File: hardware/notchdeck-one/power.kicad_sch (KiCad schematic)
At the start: 23 parts, among them J1 USB-C, J2 BAT 1S, Q1 AO3401A, U2 AP2112K-3.3, U3 MCP73832-2-OT, U4 MAX17048, U7 USBLC6-2SC6

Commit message: Add keyed harnesses and build plan for Japanese-style dual and mascon handles
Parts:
- J2: BOM Comments Mating harnesses not included. J2: protected 1S cell, pin 1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 -> Two-pin JST PH battery connector. Pin1=BAT+, pin2=GND. Mati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
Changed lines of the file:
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@@
 		(title "NotchDeck One — Power and battery")
 		(date "2026-10-03")
-		(rev "C")
+		(rev "D")
 		(company "BenchBits")
 	)
@@
 			(effects (font (size 1.27 1.27))) (hide yes)
 		)
-		(property "BOM Comments" "Mating harnesses not included. J2: protected 1S cell, pin 1 positive / pin 2 ground. J5-J8: lever signal / ground."
+		(property "BOM Comments" "Two-pin JST PH battery connector. Pin1=BAT+, pin2=GND. Mating harness separate."
 			(at 182.8800 167.6400 0)
 			(effects (font (size 1.27 1.27))) (hide yes)

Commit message: Add protected PWM actuator outputs and charger interlock
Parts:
- added Q6: 2N7002, Package_TO_SOT_SMD:SOT-23, symbol Transistor_FET:2N7002
- added R59: 100k, Resistor_SMD:R_0402_1005Metric, symbol Device:R
- J2: BOM Checked 2026-10-03 -> 2026-10-05
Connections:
- net +3V3: now also R59.1
- net GND: now also Q6.2 (S); no longer R3.2
- net BAT+ renamed BAT_RAW
- new net: Q6.3 (D), R3.2
- new net CHARGE_ENABLE: Q6.1 (G), R59.2
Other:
- note added: "U3 is MCP73832 (open-drain STAT), not MCP73831. R3 = 2k: nominal 500mA charge. Q6 opens PROG return during actuation. J2: protected 1S Li-ion pack, pin 1 positive, pin 2 GND. Match cell/USB budget; bench-check Q6 charge current and off leakage."
- note removed: "U3 is MCP73832 (open-drain STAT), not MCP73831. R3 = 2k: 500mA charge. Match cell and USB source budget. J2: protected 1S Li-ion pack, pin 1 positive, pin 2 GND."

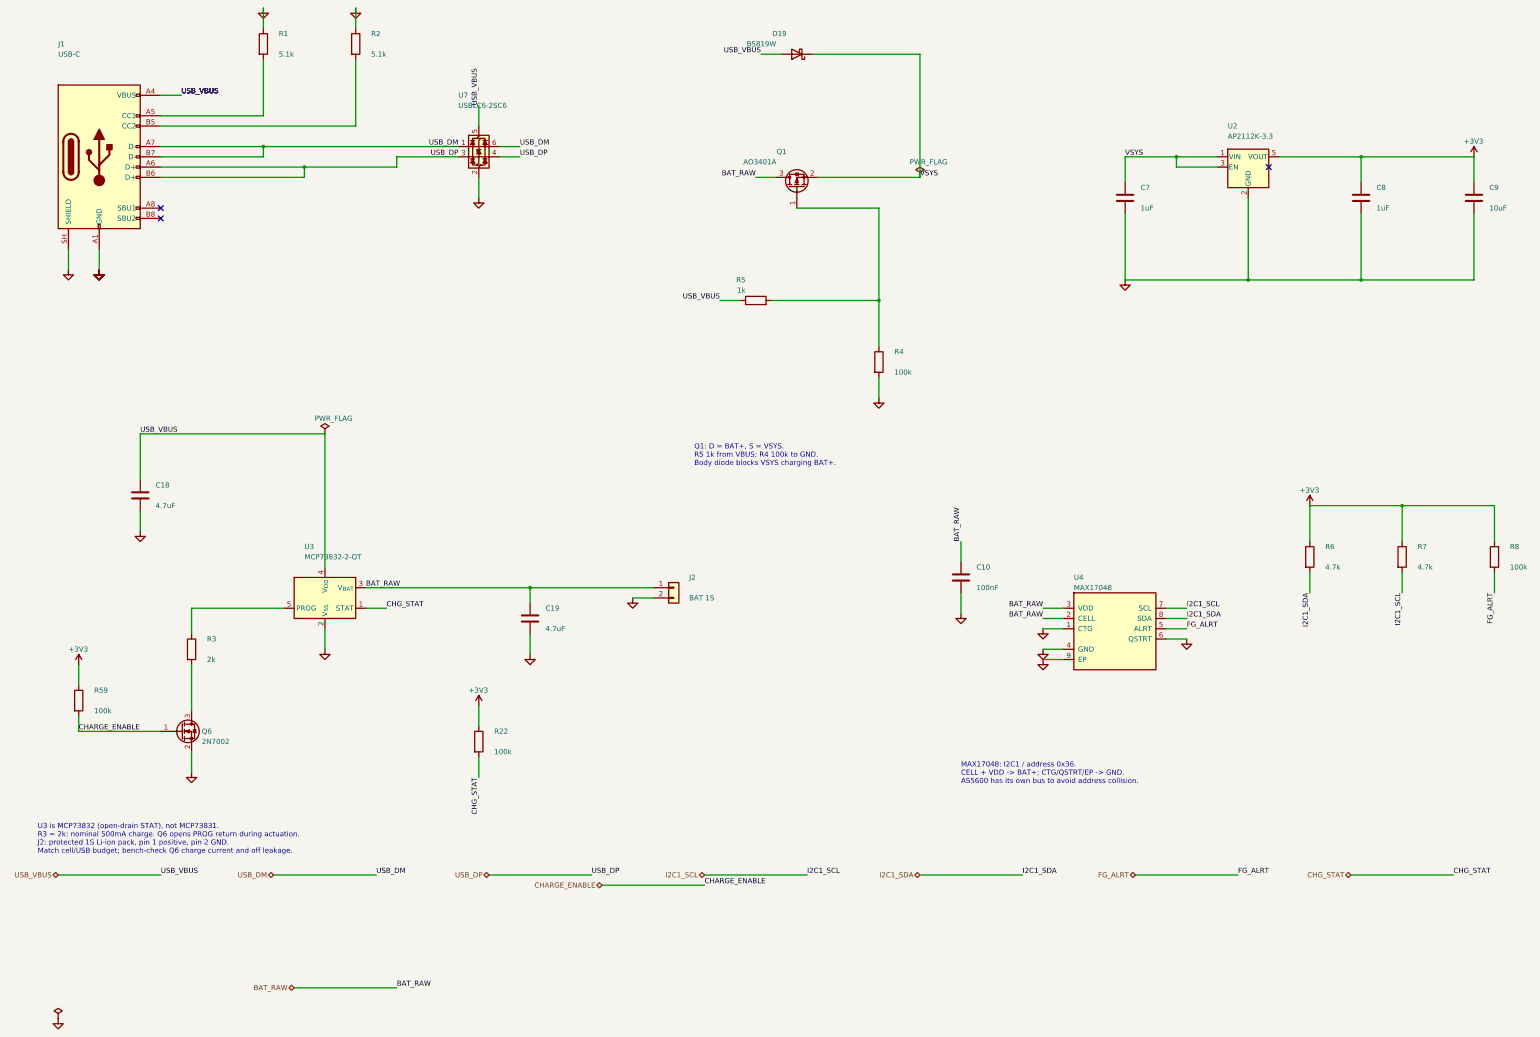
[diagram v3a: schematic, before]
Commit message: Protect full battery input and size dual 2A impulse outputs
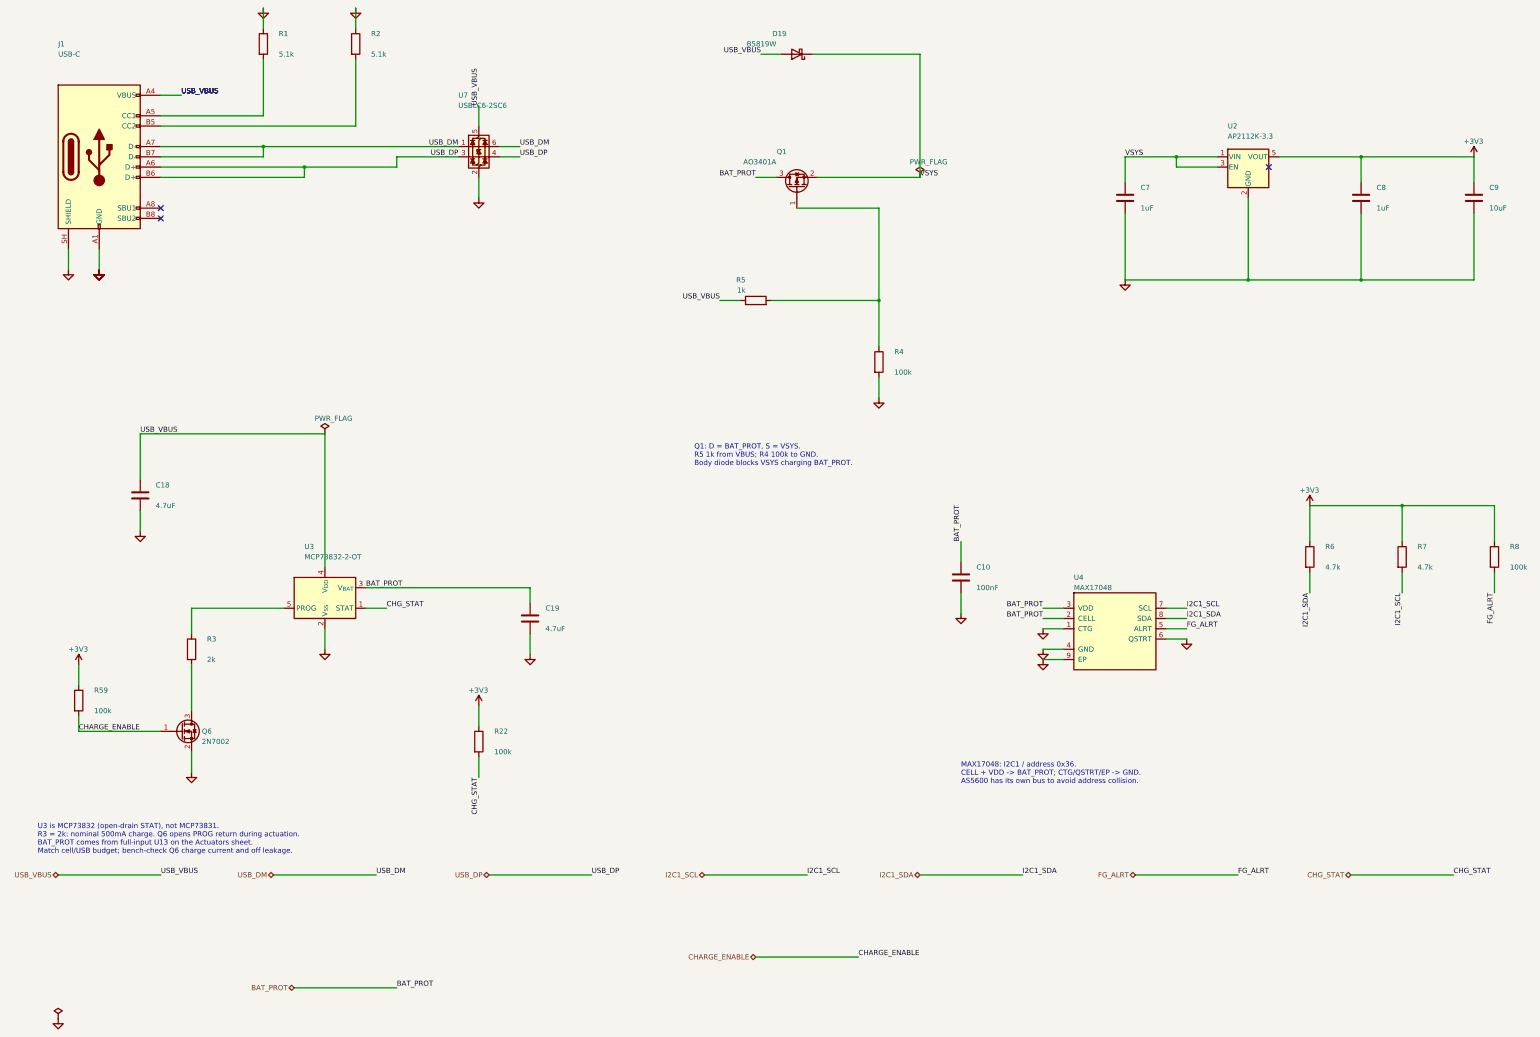
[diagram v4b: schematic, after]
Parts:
- removed J2: BAT 1S, Connector_JST:JST_PH_S2B-PH-SM4-TB_1x02-1MP_P2.00mm_Horizontal, symbol Connector_Generic:Conn_01x02
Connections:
- net BAT_RAW renamed BAT_PROT
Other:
- note added: "MAX17048: I2C1 / address 0x36. CELL + VDD -> BAT_PROT; CTG/QSTRT/EP -> GND. AS5600 has its own bus to avoid address collision."
- note added: "Q1: D = BAT_PROT, S = VSYS. R5 1k from VBUS; R4 100k to GND. Body diode blocks VSYS charging BAT_PROT."
- note added: "U3 is MCP73832 (open-drain STAT), not MCP73831. R3 = 2k: nominal 500mA charge. Q6 opens PROG return during actuation. BAT_PROT comes from full-input U13 on the Actuators sheet. Match cell/USB budget; bench-check Q6 charge current and off leakage."
- note removed: "MAX17048: I2C1 / address 0x36. CELL + VDD -> BAT+; CTG/QSTRT/EP -> GND. AS5600 has its own bus to avoid address collision."
- note removed: "Q1: D = BAT+, S = VSYS. R5 1k from VBUS; R4 100k to GND. Body diode blocks VSYS charging BAT+."
- note removed: "U3 is MCP73832 (open-drain STAT), not MCP73831. R3 = 2k: nominal 500mA charge. Q6 opens PROG return during actuation. J2: protected 1S Li-ion pack, pin 1 positive, pin 2 GND. Match cell/USB budget; bench-check Q6 charge current and off leakage."
